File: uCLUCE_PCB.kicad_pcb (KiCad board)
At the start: 2 copper layers, 3 parts, among them P1 USB_A, U1 PIC16F1455-I/ST, U2 MCP2003B

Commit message: Coponents add
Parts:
- added C1: 0.47u, Capacitors_SMD:C_0603, F.Cu at (54.6, 41.9)
- added C2: 100n, Capacitors_SMD:C_0603, F.Cu at (54.6, 44.5)
- added C3: 100n, Capacitors_SMD:C_0603, F.Cu at (54.6, 47.0)
- added D1: D, Diodes_SMD:D_0805, F.Cu at (54.6, 30.5)
- added ICS1: Conn_01x05, Pin_Headers:Pin_Header_Straight_1x05_Pitch2.54mm, B.Cu at (40.6, 46.4)
- added J1: Screw_Terminal_01x03, Connectors:AK300-3, B.Cu at (41.9, 30.5)
- added J2: GS2, Connectors:GS2, F.Cu at (54.6, 38.1)
- added R1: 1k, Resistors_SMD:R_0603, F.Cu at (54.6, 34.3)
- P1: moved to B.Cu
- moved U1 118.1 mm to (47.6, 43.8), turned to 180 degrees
- moved U2 117.5 mm to (47.6, 36.8)
- moved P1 111.4 mm to (51.4, 49.5), turned to 180 degrees
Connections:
- P1 pad 1: (no net) -> +5V
- P1 pad 2: (no net) -> Net-(P1-Pad2)
- P1 pad 3: (no net) -> Net-(P1-Pad3)
- P1 pad 4: (no net) -> GND
- P1 pad 5: Net-(P1-Pad5) -> GND
- U1 pad 1: (no net) -> +5V
- U1 pad 10: (no net) -> Net-(ICS1-Pad2)
- U1 pad 11: (no net) -> Net-(C1-Pad2)
- U1 pad 12: (no net) -> Net-(P1-Pad2)
- U1 pad 13: (no net) -> Net-(P1-Pad3)
- U1 pad 14: (no net) -> GND
- U1 pad 2: (no net) -> Net-(U1-Pad2)
- U1 pad 3: (no net) -> Net-(U1-Pad3)
- U1 pad 4: (no net) -> /MCLR
- U1 pad 5: (no net) -> Net-(U1-Pad5)
- U1 pad 6: (no net) -> Net-(U1-Pad6)
- U1 pad 7: (no net) -> Net-(U1-Pad7)
- U1 pad 8: (no net) -> Net-(U1-Pad8)
- U1 pad 9: (no net) -> Net-(ICS1-Pad1)
- U2 pad 1: (no net) -> Net-(U1-Pad6)
- U2 pad 2: (no net) -> Net-(U1-Pad7)
- U2 pad 3: (no net) -> Net-(U1-Pad3)
- U2 pad 4: (no net) -> Net-(U1-Pad5)
- U2 pad 5: (no net) -> GND
- U2 pad 6: (no net) -> Net-(J1-Pad2)
- U2 pad 7: (no net) -> +BATT
- U2 pad 8: (no net) -> Net-(U2-Pad8)
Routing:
- net +BATT: track 0.00 -> 20.7 mm, vias 0 -> 1
- net Net-(J1-Pad2): track 0.00 -> 14.4 mm
- net Net-(U1-Pad3): track 0.00 -> 13.8 mm
- net Net-(U1-Pad6): track 0.00 -> 13.2 mm
- net GND: track 0.00 -> 10.4 mm
- net Net-(U1-Pad7): track 0.00 -> 9.69 mm
- net +5V: track 0.00 -> 9.39 mm
- net Net-(U1-Pad5): track 0.00 -> 8.84 mm
- net Net-(P1-Pad2): track 0.00 -> 8.83 mm
- net Net-(P1-Pad3): track 0.00 -> 6.32 mm
- net Net-(ICS1-Pad2): track 0.00 -> 4.30 mm
- net Net-(J2-Pad1): track 0.00 -> 2.42 mm
- net Net-(D1-Pad1): track 0.00 -> 2.01 mm
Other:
- board outline added: 17.8 x 27.9 mm

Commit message: Route
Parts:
- added C4: 220p, Capacitors_SMD:C_0603, F.Cu at (54.5, 38.5)
- added C5: 1u, Capacitors_SMD:C_0603, F.Cu at (54.0, 33.1)
- added R2: 4,7k, Resistors_SMD:R_0603, F.Cu at (41.2, 34.0)
- C2: value 100n -> 470n
- moved J2 2.33 mm to (55.5, 36.0)
- moved ICS1 1.88 mm to (41.0, 48.2)
- moved R1 1.75 mm to (55.9, 33.1)
- moved D1 1.28 mm to (54.8, 29.2)
- moved C1 1.10 mm to (54.6, 43.0)
- moved C2 0.56 mm to (54.6, 45.0)
- moved U2 0.17 mm to (47.8, 36.8)
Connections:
- U1 pad 2: Net-(U1-Pad2) -> (no net)
- U1 pad 8: Net-(U1-Pad8) -> (no net)
- U2 pad 8: Net-(U2-Pad8) -> (no net)
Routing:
- net GND: track 10.4 -> 76.3 mm, vias 0 -> 1
- net +5V: track 9.39 -> 28.7 mm
- net /MCLR: track 0.00 -> 18.1 mm, vias 0 -> 1
- net Net-(C1-Pad2): track 0.12 -> 12.1 mm, vias 0 -> 2
- net Net-(ICS1-Pad1): track 0.00 -> 8.69 mm, vias 0 -> 1
- net Net-(C4-Pad2): track 14.4 -> 17.3 mm
- net Net-(R2-Pad1): track 13.2 -> 15.9 mm
- net +BATT: track 20.7 -> 23.4 mm
- net Net-(J2-Pad1): track 2.42 -> 1.64 mm
- net Net-(U1-Pad3): track 13.8 -> 13.1 mm
- net Net-(D1-Pad1): track 2.01 -> 2.53 mm
- added copper zone on B.Cu, net GND
- added copper zone on F.Cu, net GND
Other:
- board size 17.8 x 27.9 mm -> 17.8 x 28 mm
- board text added: "BAT"
- board text added: "CAN DEVICES"
- board text added: "GND"
- board text added: "LIN"
- board text added: "LUC 0.1"
- board text added: "U"

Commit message: diodes add
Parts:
- added D2: D_Schottky_Small, Diodes_SMD:D_SMA, F.Cu at (49.5, 30.9)
- added D3: SMBD914E6327HTSA1, Diodes_SMD:D_SOT-23_ANK, F.Cu at (44.1, 33.3)
- added R3: 50, Resistors_SMD:R_0603, F.Cu at (41.0, 33.3)
- D1: value D -> SMBD914E6327HTSA1; footprint Diodes_SMD:D_0805 -> Diodes_SMD:D_SOT-23_ANK
- J1: moved to F.Cu
- moved U2 1.62 mm to (47.8, 38.5)
- moved U1 1.34 mm to (47.6, 45.2)
- moved R2 1.15 mm to (41.2, 35.1)
- moved C4 0.74 mm to (55.1, 38.9), turned to 0 degrees
- moved J1 0.67 mm to (41.9, 29.8)
- moved D1 0.39 mm to (55.0, 29.5)
- moved R1 0.20 mm to (56.0, 33.1)
- turned C5 to 90 degrees
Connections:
- C4 pad 1: GND -> Net-(C4-Pad1)
- C4 pad 2: Net-(C4-Pad2) -> GND
- C5 pad 1: GND -> Net-(C5-Pad1)
- C5 pad 2: +BATT -> GND
- J1 pad 2: Net-(C4-Pad2) -> Net-(C4-Pad1)
- J2 pad 2: Net-(C4-Pad2) -> Net-(C4-Pad1)
- U2 pad 6: Net-(C4-Pad2) -> Net-(C4-Pad1)
- U2 pad 7: +BATT -> Net-(C5-Pad1)
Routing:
- net Net-(C5-Pad1): track 0.00 -> 28.1 mm, vias 0 -> 2
- net Net-(C4-Pad1): track 0.00 -> 18.8 mm
- net Net-(C4-Pad2): track 17.3 -> 0.00 mm
- net Net-(P1-Pad3): track 6.32 -> 4.55 mm
- net Net-(P1-Pad2): track 8.83 -> 7.14 mm
- net Net-(D1-Pad1): track 2.53 -> 4.15 mm
- net Net-(D3-Pad1): track 0.00 -> 1.37 mm
- net Net-(ICS1-Pad1): track 8.69 -> 7.42 mm
- net +BATT: track 23.4 -> 22.2 mm, vias 1 -> 0
- net /MCLR: track 18.1 -> 17.2 mm
- net Net-(U1-Pad5): track 8.84 -> 8.19 mm
- net +5V: track 28.7 -> 29.3 mm
- net Net-(ICS1-Pad2): track 4.65 -> 4.10 mm
- net Net-(C1-Pad2): track 12.1 -> 12.6 mm

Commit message: Footprint update
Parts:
- added P2: UART_TTL, Pin_Headers:Pin_Header_Straight_1x02_Pitch2.54mm, F.Cu at (54.5, 43.0)
- added U3: fiducial, Fiducials:Fiducial_1mm_Dia_2.54mm_Outer_CopperBottom, B.Cu at (47.9, 52.3)
- P1: footprint Connect:USB_A -> uCLUCE_PCB:USB_A_DS1097
- moved C1 11.4 mm to (43.8, 46.6), turned to 90 degrees
- moved R3 5.88 mm to (46.9, 34.3), turned to 180 degrees
- moved C2 1.60 mm to (54.6, 46.6)
- moved C4 1.29 mm to (54.9, 37.6)
- moved C3 1.20 mm to (54.6, 48.2)
- moved C5 1.14 mm to (52.9, 33.4)
- moved U1 1.10 mm to (48.7, 45.2)
- moved D3 0.96 mm to (44.9, 32.7), turned to 0 degrees
- moved R1 0.87 mm to (55.6, 32.3)
- moved R2 0.81 mm to (41.6, 34.4), turned to 270 degrees
- moved ICS1 0.71 mm to (41.5, 47.6)
- moved J2 0.69 mm to (55.4, 35.3)
- moved D1 0.55 mm to (55.0, 29.0)
- moved J1 0.25 mm to (41.9, 29.6)
- moved D2 0.15 mm to (49.5, 30.8)
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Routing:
- net /MCLR: track 17.2 -> 36.0 mm, vias 1 -> 0
- net Net-(C5-Pad1): track 28.1 -> 13.9 mm, vias 2 -> 0
- net Net-(C1-Pad2): track 12.6 -> 2.24 mm, vias 2 -> 0
- net GND: track 76.8 -> 87.0 mm, vias 1 -> 0
- net Net-(P2-Pad1): track 8.19 -> 13.9 mm
- net Net-(P2-Pad2): track 15.4 -> 21.1 mm
- net Net-(ICS1-Pad1): track 7.42 -> 11.1 mm, vias 1 -> 0
- net +BATT: track 22.2 -> 19.4 mm
- net Net-(U1-Pad3): track 13.4 -> 14.9 mm
- net Net-(C4-Pad1): track 18.8 -> 20.2 mm
- net +5V: track 29.3 -> 28.0 mm
- net Net-(ICS1-Pad2): track 4.10 -> 5.20 mm
- net Net-(P1-Pad2): track 7.14 -> 6.10 mm
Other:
- board size 17.8 x 28 mm -> 17.1 x 27.5 mm
- board text added: "RX"
- board text added: "TX"

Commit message: footprint update
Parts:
- U2: value MCP2003B -> MCP2003B-E/SN; footprint Housings_SOIC:SO-8_5.3x6.2mm_Pitch1.27mm -> Housings_SOIC:SOIC-8_3.9x4.9mm_Pitch1.27mm
- moved U2 0.31 mm to (47.9, 38.8)
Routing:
- net Net-(C4-Pad1): track 20.2 -> 23.4 mm
- net Net-(C5-Pad1): track 13.9 -> 15.4 mm
- net Net-(U1-Pad3): track 14.9 -> 13.7 mm
- net /MCLR: track 36.0 -> 36.9 mm
- net Net-(P2-Pad1): track 13.9 -> 13.0 mm
- removed copper zone on B.Cu, net GND

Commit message: gerber generation
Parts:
- P2: footprint Pin_Headers:Pin_Header_Straight_1x02_Pitch2.54mm -> Pin_Headers:Pin_Header_Straight_1x03_Pitch2.54mm
- moved C4 1.68 mm to (53.5, 36.6), turned to 270 degrees
- moved P2 1.58 mm to (54.5, 44.6)
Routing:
- net GND: track 87.4 -> 90.5 mm
- net Net-(C4-Pad1): track 23.4 -> 20.6 mm
- net /MCLR: track 36.9 -> 35.2 mm
- net Net-(P2-Pad1): track 13.0 -> 11.3 mm

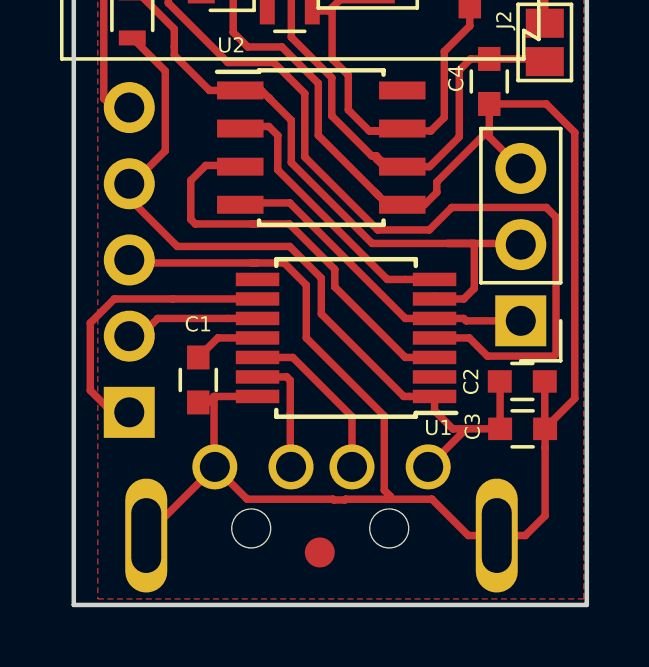
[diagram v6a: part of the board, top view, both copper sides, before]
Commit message: Fixed USB Layout
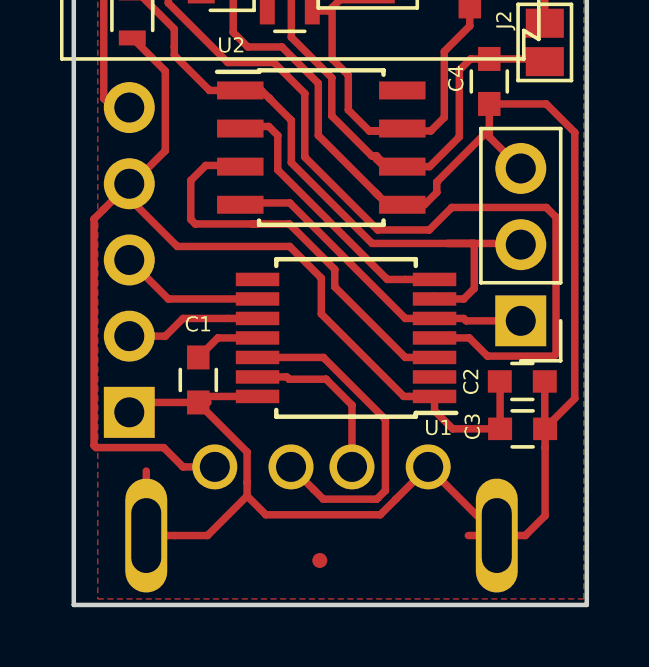
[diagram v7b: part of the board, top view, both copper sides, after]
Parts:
- P1: footprint uCLUCE_PCB:USB_A_DS1097 -> uCLUCE_PCB:USB_A_DS1097R
- U3: footprint Fiducials:Fiducial_1mm_Dia_2.54mm_Outer_CopperBottom -> uCLUCE_PCB:FICUCIAL_MIN
- moved U3 0.27 mm to (47.9, 52.6)
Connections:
- ICS1 pad 1: Net-(ICS1-Pad1) -> GND
- ICS1 pad 3: GND -> Net-(ICS1-Pad3)
- U1 pad 2: (no net) -> Net-(U1-Pad2)
- U1 pad 8: (no net) -> Net-(U1-Pad8)
- U1 pad 9: Net-(ICS1-Pad1) -> Net-(ICS1-Pad3)
- U2 pad 8: (no net) -> Net-(U2-Pad8)
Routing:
- net +5V: track 28.1 -> 40.7 mm
- net Net-(ICS1-Pad1): track 11.1 -> 0.00 mm
- net GND: track 90.5 -> 84.4 mm
- net Net-(P1-Pad2): track 6.10 -> 11.7 mm
- net Net-(ICS1-Pad3): track 0.00 -> 5.41 mm
- net Net-(P1-Pad3): track 4.09 -> 5.82 mm

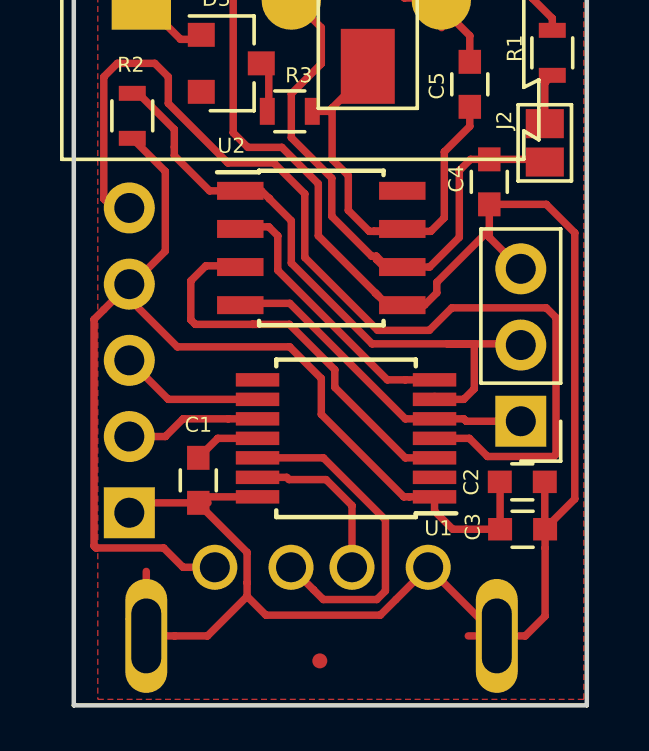
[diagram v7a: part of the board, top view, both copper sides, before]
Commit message: Flip LIN RX/TX
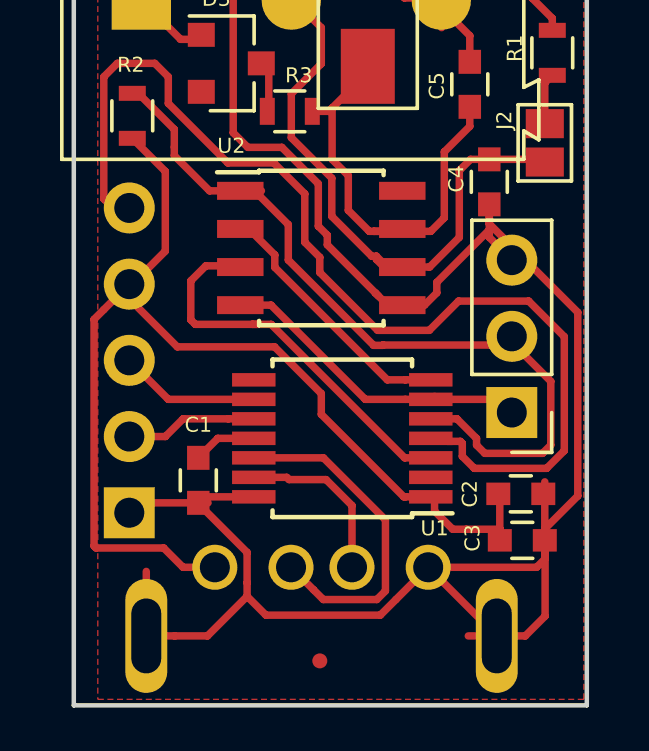
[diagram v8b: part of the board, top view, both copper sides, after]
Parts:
- moved P2 0.42 mm to (54.2, 44.3)
- moved C2 0.40 mm to (54.5, 47.0)
- moved C3 0.37 mm to (54.6, 48.6)
- moved U1 0.12 mm to (48.6, 45.2)
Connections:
- U1 pad 2: Net-(U1-Pad2) -> (no net)
- U1 pad 5: Net-(P2-Pad1) -> Net-(P2-Pad2)
- U1 pad 6: Net-(P2-Pad2) -> Net-(P2-Pad1)
- U1 pad 8: Net-(U1-Pad8) -> (no net)
- U2 pad 8: Net-(U2-Pad8) -> (no net)
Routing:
- net Net-(P2-Pad2): track 21.8 -> 27.0 mm
- net GND: track 84.4 -> 88.0 mm
- net /MCLR: track 35.2 -> 36.2 mm
- net Net-(P2-Pad1): track 11.3 -> 10.7 mm
